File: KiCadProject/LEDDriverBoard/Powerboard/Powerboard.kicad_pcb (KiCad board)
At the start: 4 copper layers, 45 x 45 mm, 28 parts, among them J1 XT30, J2 XT30, J3 Conn_01x03_Male, Q1 Q_NMOS_GDS, Q2 SUD50P10-43L-GE3, U1 MAX16833

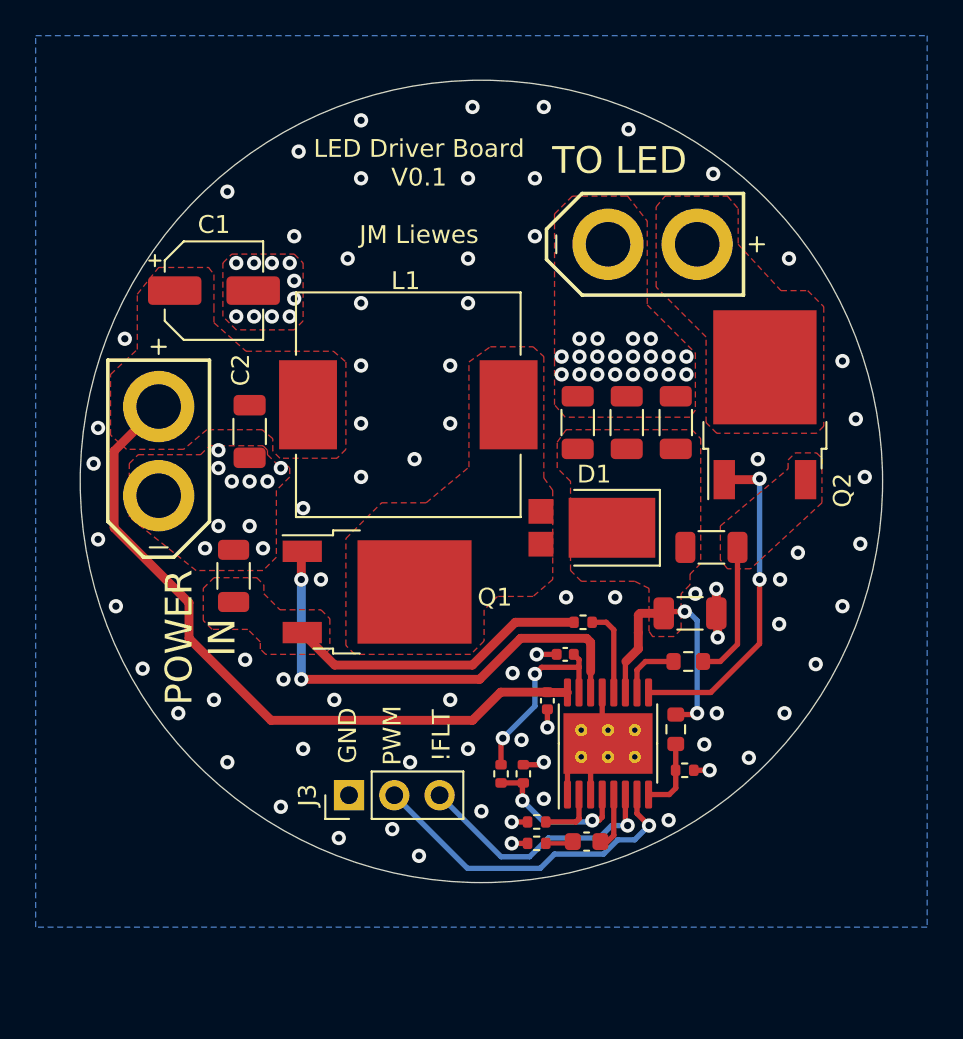
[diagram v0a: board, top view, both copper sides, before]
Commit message: Final touches before component order and PCB layout
Signed-off-by: Eldalote.Electronics <Eldalote.Electronics@gmail.com>
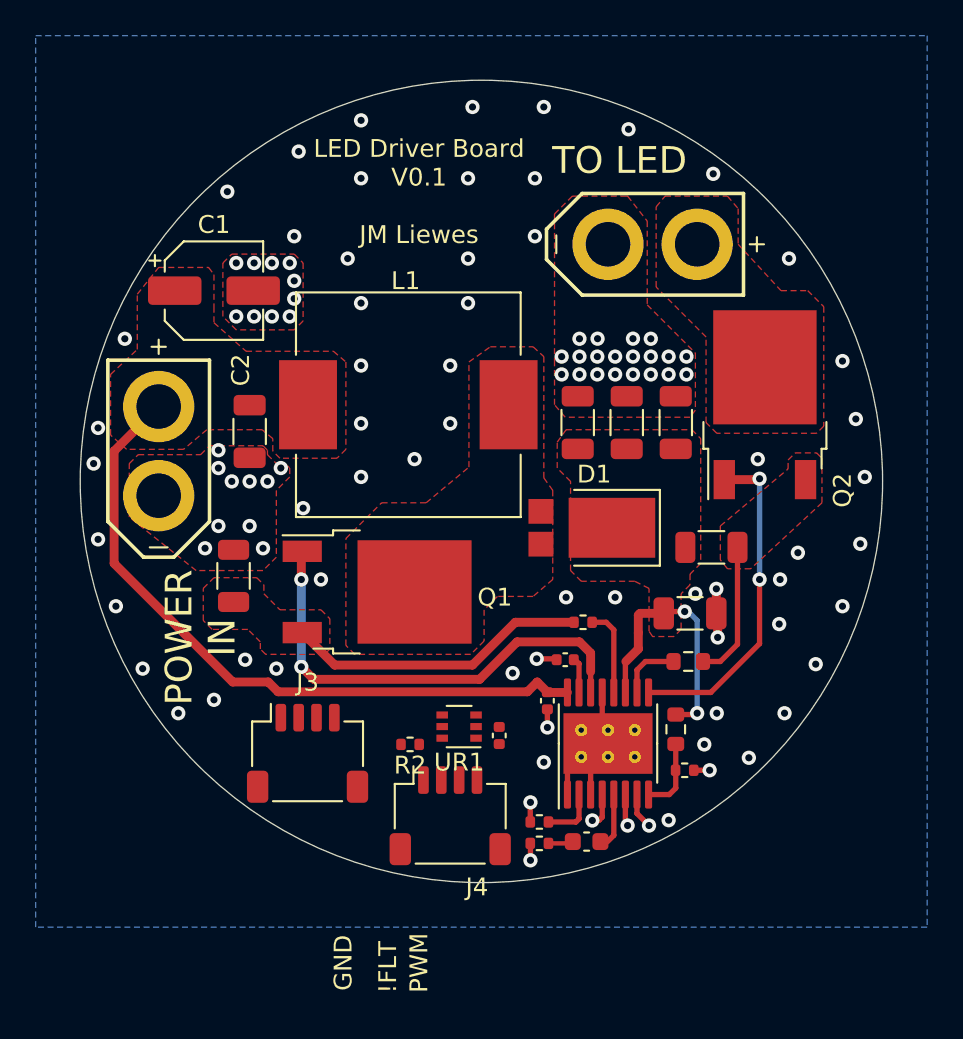
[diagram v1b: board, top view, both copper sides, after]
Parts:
- removed R3: 100k, Resistor_SMD:R_0402_1005Metric
- added C10: 100n, Capacitor_SMD:C_0402_1005Metric, F.Cu at (151.0, 114.2)
- added J4: JST_SM04B, Connector_JST:JST_SH_SM04B-SRSS-TB_1x04-1MP_P1.00mm_Horizontal, F.Cu at (148.2, 118.8)
- added UR1: MCP4018T-104E, Package_TO_SOT_SMD:SOT-363_SC-70-6, F.Cu at (148.8, 113.8)
- C4: value 2u2 -> 1u
- J3: value Conn_01x03_Male -> JST_SM04B; footprint Connector_PinHeader_2.54mm:PinHeader_1x03_P2.54mm_Vertical -> Connector_JST:JST_SH_SM04B-SRSS-TB_1x04-1MP_P1.00mm_Horizontal
- moved R2 5.36 mm to (146.0, 114.8), turned to 180 degrees
- moved J3 3.31 mm to (140.2, 115.2), turned to 0 degrees
- moved C4 0.30 mm to (154.7, 110.0)
- moved R1 0.15 mm to (153.2, 119.1)
- moved R8 0.15 mm to (153.2, 120.3)
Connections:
- J3 pad 1: GND -> +3V3
- J3 pad 2: /PWMDIM -> /I2C_SDA
- J3 pad 3: /!FTL -> /I2C_SCL
- R2 pad 1: /ICTRL -> /divider_high
- R2 pad 2: /VCC -> +3V3
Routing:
- net /PWMDIM: track 19.0 -> 2.02 mm
- net /!FTL: track 14.5 -> 1.79 mm
- net /VCC: track 10.8 -> 2.00 mm, vias 2 -> 0
- net /ICTRL: track 8.61 -> 2.02 mm, vias 2 -> 1
- net /NDRV: track 27.3 -> 26.4 mm
- net /IN: track 39.6 -> 38.7 mm
- net GND: track 17.5 -> 17.2 mm, vias 115 -> 102

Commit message: Components selected, MfID added to schematics, and components ordered
Signed-off-by: Eldalote.Electronics <Eldalote.Electronics@gmail.com>
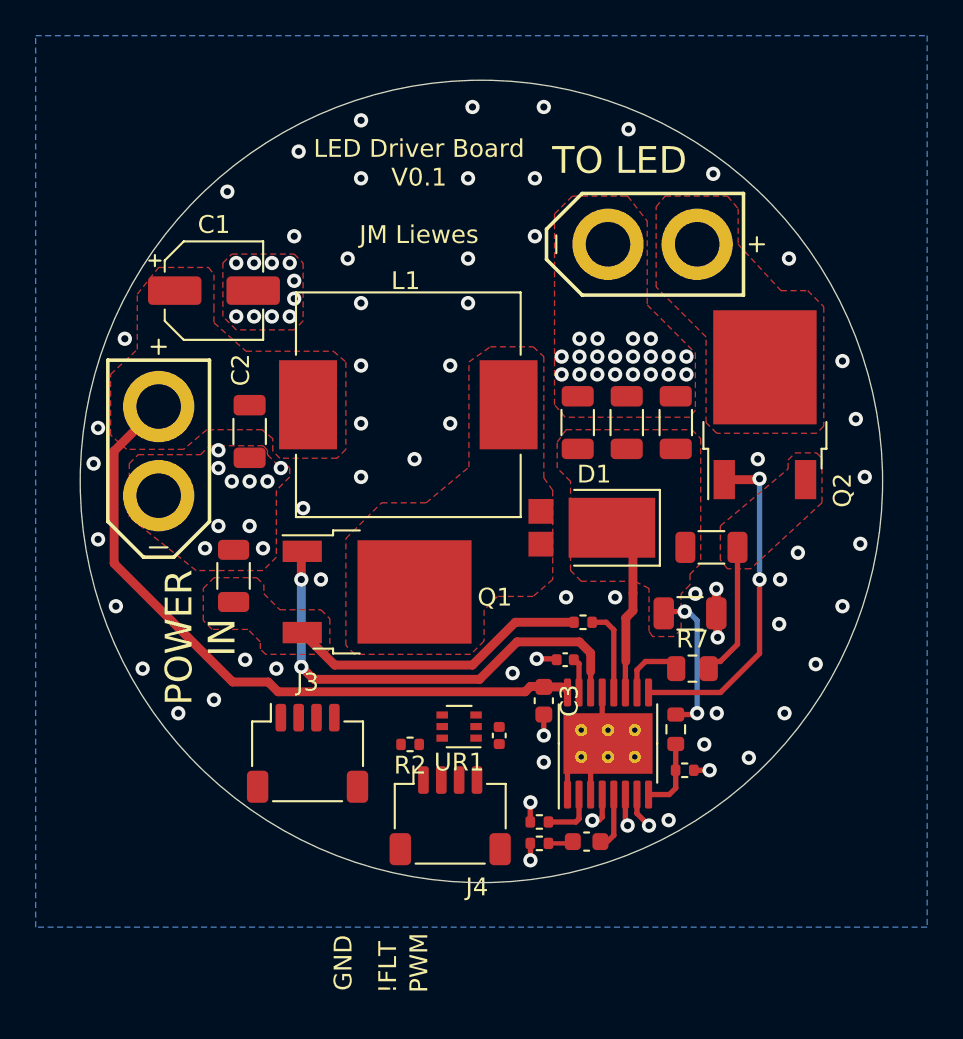
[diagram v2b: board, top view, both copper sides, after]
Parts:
- C3: footprint Capacitor_SMD:C_0402_1005Metric -> Capacitor_SMD:C_0603_1608Metric
- R1: value 7k3 -> 7k32
- R7: footprint Resistor_SMD:R_0603_1608Metric -> Resistor_SMD:R_0805_2012Metric
- moved NT1 1.29 mm to (158.5, 106.8)
- moved R7 0.47 mm to (161.8, 110.5)
- moved C3 0.20 mm to (153.5, 112.3)
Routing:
- net /V-out: track 10.0 -> 12.7 mm
- net /ISENSE+: track 3.64 -> 4.76 mm
